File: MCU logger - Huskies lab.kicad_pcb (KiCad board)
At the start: 2 copper layers, 29 parts, among them J1 Conn_01x04_Male, J2 Conn_01x04_Male, J3 Conn_02x03_Odd_Even, J4 Conn_01x09_Male, U1 ATMEGA328P-AU, U2 DS1337S+, U3 24LC1025, U4 24LC1025, Y1 32.768KHz, Y2 16Mhz

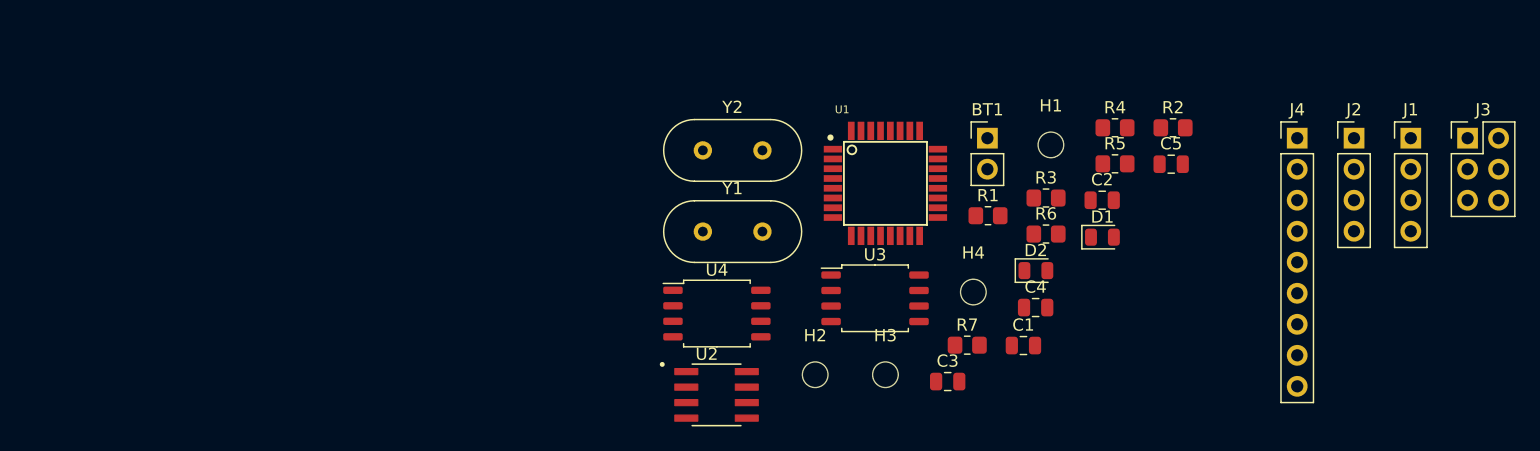
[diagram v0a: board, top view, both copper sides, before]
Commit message: colocacion de los componentes terminada
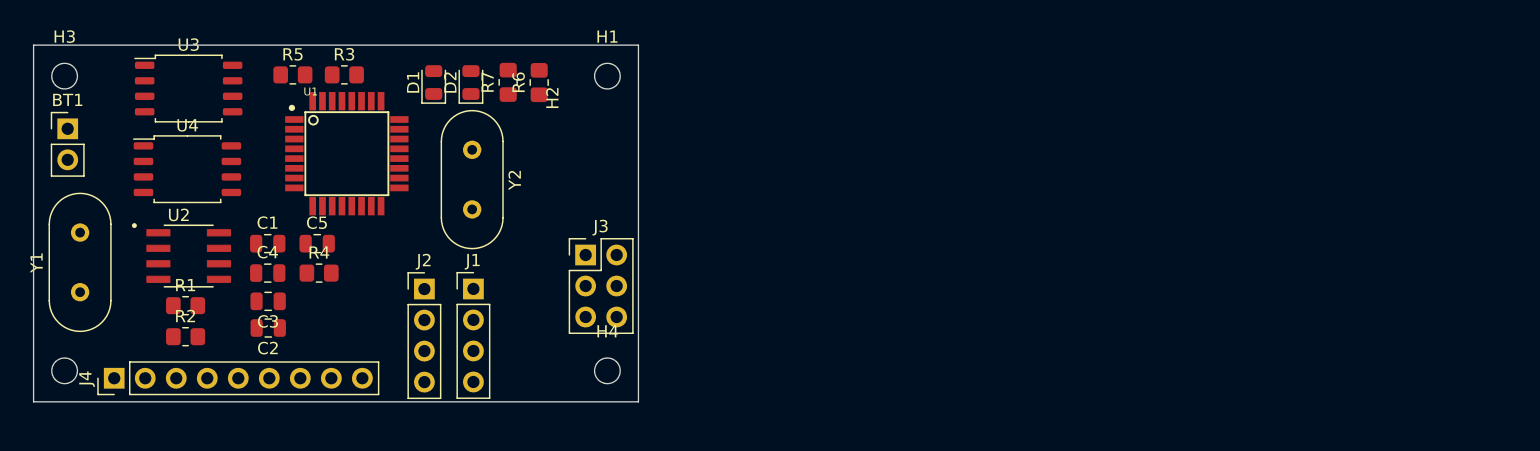
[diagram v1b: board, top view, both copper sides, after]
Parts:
- moved J4 98.8 mm to (51.1, 70.5), turned to 90 degrees
- moved R2 82.6 mm to (56.9, 67.1)
- moved J1 77.7 mm to (80.5, 63.1)
- moved J2 77.1 mm to (76.5, 63.2)
- moved BT1 75.3 mm to (47.2, 50.0)
- moved J3 72.8 mm to (89.7, 60.4)
- moved H3 71.5 mm to (47.0, 45.7)
- moved C5 70.2 mm to (67.7, 59.4)
- moved C2 69.1 mm to (63.7, 66.3), turned to 180 degrees
- moved R5 67.7 mm to (65.7, 45.6)
- moved R4 66.3 mm to (67.8, 61.8)
- moved R1 66.1 mm to (56.9, 64.5)
- moved C4 62.9 mm to (63.6, 61.8)
- moved C1 62.4 mm to (63.6, 59.4)
- moved H2 61.5 mm to (47.0, 69.8)
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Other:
- board outline added: 49.5 x 29.2 mm
